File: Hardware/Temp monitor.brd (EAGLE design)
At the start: 99 x 49 mm, 41 parts, among them IC1 74LS595D, IC2 74LS595D, IC3 74LS595D, IC4 74LS595D, IC5 74LS595D, J2 TP_8, J3 USB-MICROB, T1 NPN, T2 NPN, T3 NPN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

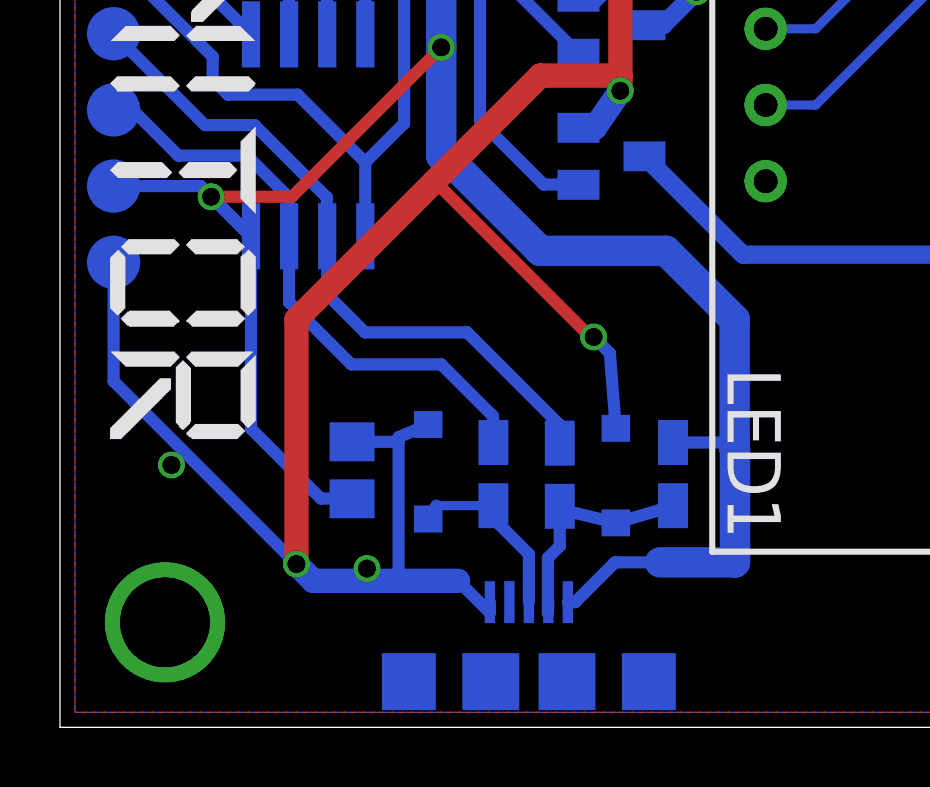
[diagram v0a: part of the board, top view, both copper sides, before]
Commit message: Cleanup + through hole usb
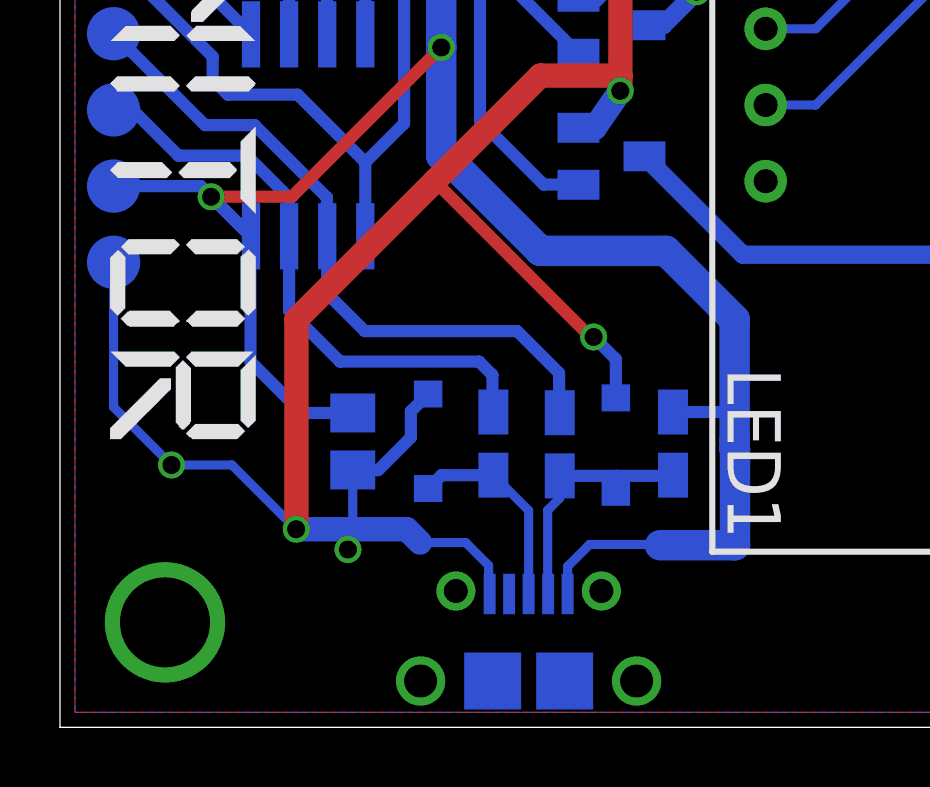
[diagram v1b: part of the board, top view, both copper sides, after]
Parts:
- J3: value USB-MICROB -> ZX62D-B-5PA8; device SparkFun-Connectors:USB-MICROB -> usb:ZX62D-B-5PA8
- moved J3 2.92 mm to (15.6, 4.45)
- moved D1 1.02 mm to (18.5, 9.41)
- moved D2 1.02 mm to (12.3, 9.54)
- moved R1 1.02 mm to (16.7, 9.44)
- moved R2 1.02 mm to (14.4, 9.46)
- moved R3 1.02 mm to (20.4, 9.46)
- moved C6 0.96 mm to (9.76, 9.53), turned to 90 degrees
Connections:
- net +5V: now also J3.VCC; no longer J3.VBUS
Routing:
- net +5V: track 214.8 -> 211.6 mm
- net GND: track 257.2 -> 255.0 mm
- net N$2: track 6.36 -> 7.17 mm
- net N$1: track 8.05 -> 8.65 mm

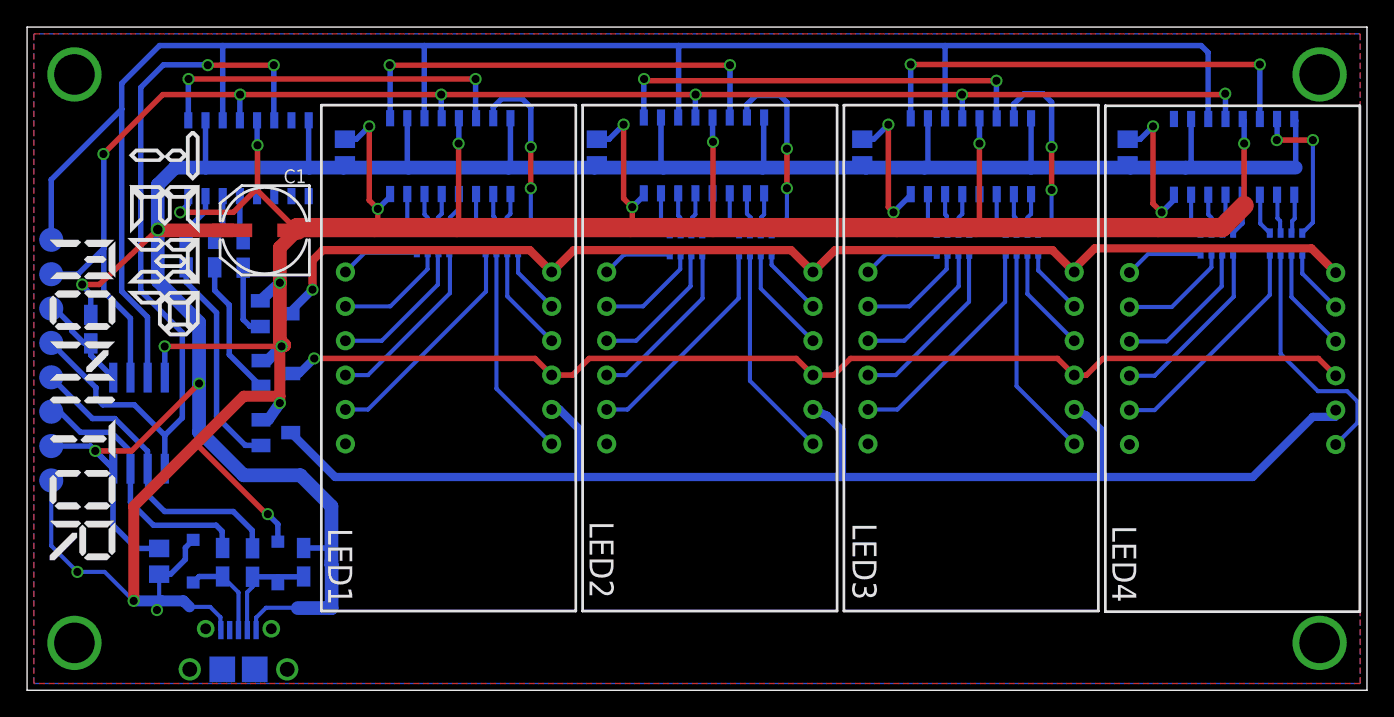
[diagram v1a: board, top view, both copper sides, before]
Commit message: Moved shift registers Board is not completed
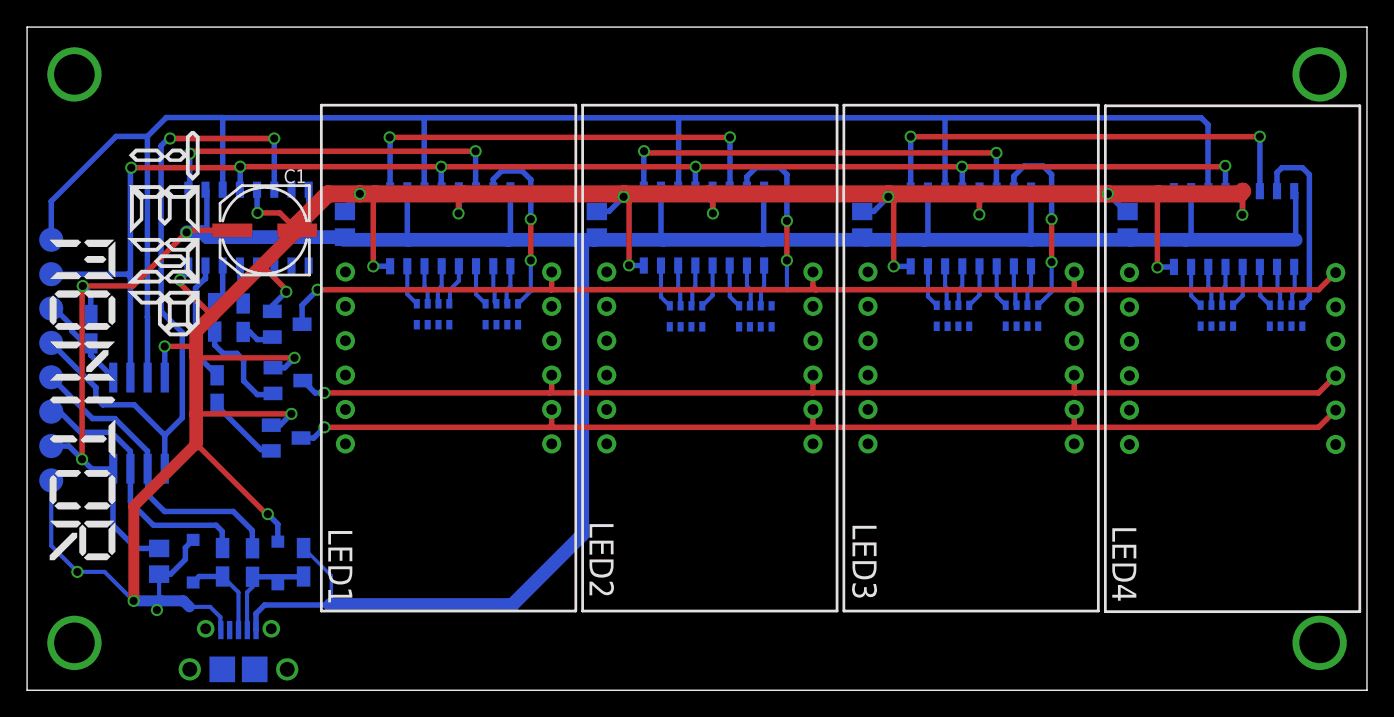
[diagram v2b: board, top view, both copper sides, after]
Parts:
- moved R6 10.3 mm to (14.0, 22.2)
- moved C2 5.33 mm to (81.3, 34.4)
- moved C3 5.33 mm to (61.7, 34.4)
- moved C4 5.33 mm to (42.1, 34.4)
- moved C5 5.33 mm to (23.5, 34.4)
- moved IC1 5.33 mm to (50.0, 34.2)
- moved IC3 5.33 mm to (69.7, 34.1)
- moved RN1 5.33 mm to (35.1, 27.8)
- moved RN2 5.33 mm to (30.0, 27.8)
- moved RN3 5.33 mm to (53.8, 27.6)
- moved RN4 5.33 mm to (48.7, 27.6)
- moved RN8 5.33 mm to (87.9, 27.7)
- moved RN6 5.33 mm to (68.4, 27.7)
- moved RN7 5.33 mm to (93.0, 27.7)
- moved IC2 5.33 mm to (31.3, 34.1)
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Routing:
- net GND: track 255.0 -> 227.8 mm
- net N$69: track 18.4 -> 0.00 mm
- net GND_D3: track 99.3 -> 81.4 mm, vias 0 -> 1
- net N$57: track 17.0 -> 0.00 mm
- net N$72: track 16.9 -> 0.00 mm
- net N$17: track 16.9 -> 0.00 mm
- net N$41: track 16.4 -> 0.00 mm
- net N$38: track 15.9 -> 0.00 mm
- net N$14: track 15.8 -> 0.00 mm
- net N$54: track 15.8 -> 0.00 mm
- net N$68: track 13.3 -> 0.00 mm
- net N$13: track 13.2 -> 0.00 mm
- net N$53: track 13.2 -> 0.00 mm
- net N$31: track 12.7 -> 0.00 mm
- net N$19: track 10.9 -> 0.00 mm
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- removed copper zone on layer 1, net GND
- removed copper zone on layer 16, net GND
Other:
- board text added: "2016 Version 1.1"
- board text removed: "2016 Version 1.0"
